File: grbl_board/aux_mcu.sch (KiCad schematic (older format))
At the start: 56 parts, among them J17 USB_B, J18 ICSP, Q5 BSS127S, Q6 BSS127S, Q7 BSS127S, SW2 SW_Push, U25 FT231XS, U26 40106, U27 74LS155, U28 ATmega328P-AU, U29 40106, U30 40106, U31 74LS153, U32 74LS153, Y2 16M

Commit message: complete footprint associations
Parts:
- removed U29, U30: 40106, symbol 4xxx:40106
- added unit 2 of U26
- added unit 3 of U26
- D47, D48: footprint (none) -> LED_SMD:LED_1206_3216Metric_Pad1.42x1.75mm_HandSolder; Digikey Part No. (none) -> 404-1042-1-ND
- U26: footprint (none) -> Package_SO:TSSOP-14_4.4x5mm_P0.65mm; Digikey Part No. (none) -> HEF40106BTT,112-ND
- U27: footprint (none) -> Package_SO:SOIC-16_3.9x9.9mm_P1.27mm; Digikey Part No. (none) -> 296-33960-5-ND
- U28: Digikey Part No. (none) -> ATMEGA328P-AU-ND
- U29: renamed from U31; footprint (none) -> Package_SO:SOIC-16_3.9x9.9mm_P1.27mm; Digikey Part No. (none) -> 296-3653-5-ND
- U30: renamed from U32; footprint (none) -> Package_SO:SOIC-16_3.9x9.9mm_P1.27mm; Digikey Part No. (none) -> 296-3653-5-ND
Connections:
- net Y_EN: now also U26.4
- net Z_EN: now also U26.6
- net at U27.10 (Q1b): now also U26.3
- net at U27.11 (Q2b): now also U26.5
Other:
- note added: "RXLED"
- note added: "TXLED"
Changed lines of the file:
@@
 F 2 "Package_QFP:TQFP-32_7x7mm_P0.8mm" H 5300 2650 50  0001 C CIN
 F 3 "http://ww1.microchip.com/downloads/en/DeviceDoc/ATmega328_P%20AVR%20MCU%20with%20picoPower%20Technology%20Data%20Sheet%2040001984A.pdf" H 5300 2650 50  0001 C CNN
+F 4 "ATMEGA328P-AU-ND" H 5300 2650 50  0001 C CNN "Digikey Part No."
 	1    5300 2650
 	1    0    0    -1
@@
 F 0 "D47" V 3547 6280 50  0000 L CNN
 F 1 "LED" V 3638 6280 50  0000 L CNN
-F 2 "" H 3600 6200 50  0001 C CNN
-F 3 "~" H 3600 6200 50  0001 C CNN
+F 2 "LED_SMD:LED_1206_3216Metric_Pad1.42x1.75mm_HandSolder" H 3600 6200 50  0001 C CNN
+F 3 "https://media.digikey.com/pdf/Data%20Sheets/Stanley%20Electric%20PDFs/1101W_Series.pdf" H 3600 6200 50  0001 C CNN
+F 4 "404-1042-1-ND" H 3600 6200 50  0001 C CNN "Digikey Part No."
 	1    3600 6200
 	0    1    1    0
@@
 F 0 "D48" V 3897 6280 50  0000 L CNN
 F 1 "LED" V 3988 6280 50  0000 L CNN
-F 2 "" H 3950 6200 50  0001 C CNN
-F 3 "~" H 3950 6200 50  0001 C CNN
+F 2 "LED_SMD:LED_1206_3216Metric_Pad1.42x1.75mm_HandSolder" H 3950 6200 50  0001 C CNN
+F 3 "https://media.digikey.com/pdf/Data%20Sheets/Stanley%20Electric%20PDFs/1101W_Series.pdf" H 3950 6200 50  0001 C CNN
+F 4 "404-1042-1-ND" H 3950 6200 50  0001 C CNN "Digikey Part No."
 	1    3950 6200
 	0    1    1    0
@@
 F 0 "U27" H 5350 7050 50  0000 C CNN
 F 1 "74LS155" H 5450 6950 50  0000 C CNN
-F 2 "" H 5200 6350 50  0001 C CNN
+F 2 "Package_SO:SOIC-16_3.9x9.9mm_P1.27mm" H 5200 6350 50  0001 C CNN
 F 3 "http://www.ti.com/lit/gpn/sn74LS155" H 5200 6350 50  0001 C CNN
+F 4 "296-33960-5-ND" H 5200 6350 50  0001 C CNN "Digikey Part No."
 	1    5200 6350
 	1    0    0    -1
@@
 F 0 "U26" H 6200 6367 50  0000 C CNN
 F 1 "40106" H 6200 6276 50  0000 C CNN
-F 2 "" H 6200 6050 50  0001 C CNN
+F 2 "Package_SO:TSSOP-14_4.4x5mm_P0.65mm" H 6200 6050 50  0001 C CNN
 F 3 "https://assets.nexperia.com/documents/data-sheet/HEF40106B.pdf" H 6200 6050 50  0001 C CNN
+F 4 "HEF40106BTT,112-ND" H 6200 6050 50  0001 C CNN "Digikey Part No."
 	1    6200 6050
-	1    0    0    -1
-$EndComp
-$Comp
-L 4xxx:40106 U29
-U 1 1 6201B7B4
-P 6200 6550
-F 0 "U29" H 6200 6867 50  0000 C CNN
-F 1 "40106" H 6200 6776 50  0000 C CNN
-F 2 "" H 6200 6550 50  0001 C CNN
-F 3 "https://assets.nexperia.com/documents/data-sheet/HEF40106B.pdf" H 6200 6550 50  0001 C CNN
-	1    6200 6550
-	1    0    0    -1
-$EndComp
-$Comp
-L 4xxx:40106 U30
-U 1 1 62027074
-P 6200 7050
-F 0 "U30" H 6200 7367 50  0000 C CNN
-F 1 "40106" H 6200 7276 50  0000 C CNN
-F 2 "" H 6200 7050 50  0001 C CNN
-F 3 "https://assets.nexperia.com/documents/data-sheet/HEF40106B.pdf" H 6200 7050 50  0001 C CNN
-	1    6200 7050
 	1    0    0    -1
 $EndComp
@@
 F 0 "U26" H 4430 3296 50  0000 L CNN
 F 1 "40106" H 4430 3205 50  0000 L CNN
-F 2 "" H 4200 3250 50  0001 C CNN
+F 2 "Package_SO:TSSOP-14_4.4x5mm_P0.65mm" H 4200 3250 50  0001 C CNN
 F 3 "https://assets.nexperia.com/documents/data-sheet/HEF40106B.pdf" H 4200 3250 50  0001 C CNN
+F 4 "HEF40106BTT,112-ND" H 4200 3250 50  0001 C CNN "Digikey Part No."
 	7    4200 3250
 	1    0    0    -1
@@
 $EndComp
 $Comp
-L 74xx:74LS153 U31
+L 74xx:74LS153 U29
 U 1 1 618CA113
 P 8350 4300
-F 0 "U31" H 8500 5300 50  0000 C CNN
+F 0 "U29" H 8500 5300 50  0000 C CNN
 F 1 "74LS153" H 8600 5200 50  0000 C CNN
-F 2 "" H 8350 4300 50  0001 C CNN
+F 2 "Package_SO:SOIC-16_3.9x9.9mm_P1.27mm" H 8350 4300 50  0001 C CNN
 F 3 "http://www.ti.com/lit/gpn/sn74LS153" H 8350 4300 50  0001 C CNN
+F 4 "296-3653-5-ND" H 8350 4300 50  0001 C CNN "Digikey Part No."
 	1    8350 4300
 	1    0    0    -1
@@
 	7850 5100 6950 5100
 $Comp
-L 74xx:74LS153 U32
+L 74xx:74LS153 U30
 U 1 1 61E49967
 P 10450 4700
-F 0 "U32" H 10600 5700 50  0000 C CNN
+F 0 "U30" H 10600 5700 50  0000 C CNN
 F 1 "74LS153" H 10700 5600 50  0000 C CNN
-F 2 "" H 10450 4700 50  0001 C CNN
+F 2 "Package_SO:SOIC-16_3.9x9.9mm_P1.27mm" H 10450 4700 50  0001 C CNN
 F 3 "http://www.ti.com/lit/gpn/sn74LS153" H 10450 4700 50  0001 C CNN
+F 4 "296-3653-5-ND" H 10450 4700 50  0001 C CNN "Digikey Part No."
 	1    10450 4700
 	1    0    0    -1
@@
 	1    0    0    -1
 $EndComp
+$Comp
+L 4xxx:40106 U26
+U 2 1 61AE43E8
+P 6200 6550
+F 0 "U26" H 6200 6867 50  0000 C CNN
+F 1 "40106" H 6200 6776 50  0000 C CNN
+F 2 "Package_SO:TSSOP-14_4.4x5mm_P0.65mm" H 6200 6550 50  0001 C CNN
+F 3 "https://assets.nexperia.com/documents/data-sheet/HEF40106B.pdf" H 6200 6550 50  0001 C CNN
+F 4 "HEF40106BTT,112-ND" H 6200 6550 50  0001 C CNN "Digikey Part No."
+	2    6200 6550
+	1    0    0    -1
+$EndComp
+$Comp
+L 4xxx:40106 U26
+U 3 1 61AE6394
+P 6200 7050
+F 0 "U26" H 6200 7367 50  0000 C CNN
+F 1 "40106" H 6200 7276 50  0000 C CNN
+F 2 "Package_SO:TSSOP-14_4.4x5mm_P0.65mm" H 6200 7050 50  0001 C CNN
+F 3 "https://assets.nexperia.com/documents/data-sheet/HEF40106B.pdf" H 6200 7050 50  0001 C CNN
+F 4 "HEF40106BTT,112-ND" H 6200 7050 50  0001 C CNN "Digikey Part No."
+	3    6200 7050
+	1    0    0    -1
+$EndComp
+Text Notes 4000 6000 0    50   ~ 0
+TXLED
+Text Notes 3650 6000 0    50   ~ 0
+RXLED
 $EndSCHEMATC

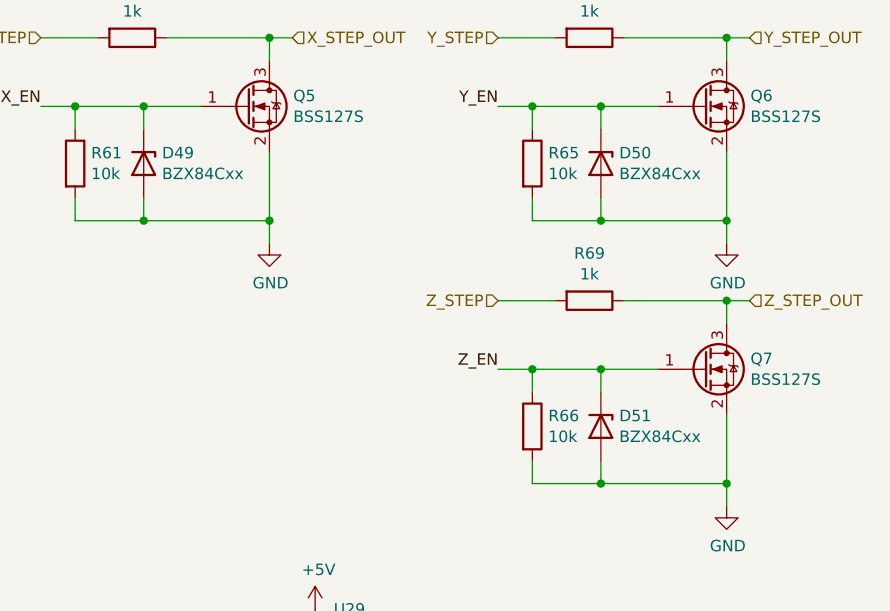
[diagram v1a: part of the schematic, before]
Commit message: fixed mismatch for 6n137
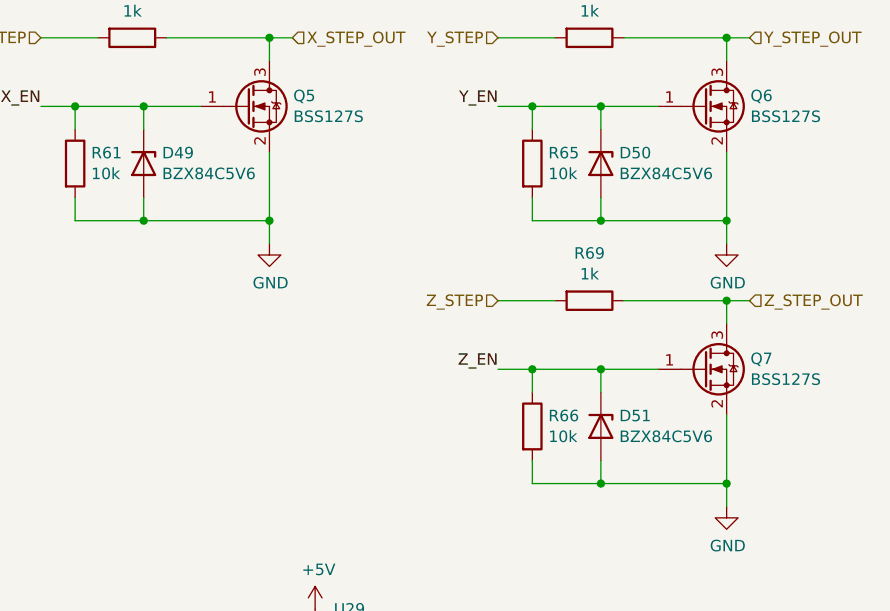
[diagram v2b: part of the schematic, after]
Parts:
- D49, D50, D51: value BZX84Cxx -> BZX84C5V6; Digikey Part No. (none) -> 1514-BZX84C5V6TRPBFREECT-ND
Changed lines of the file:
@@
 P 7600 1350
 F 0 "D49" V 7554 1430 50  0000 L CNN
-F 1 "BZX84Cxx" V 7645 1430 50  0000 L CNN
+F 1 "BZX84C5V6" V 7645 1430 50  0000 L CNN
 F 2 "Diode_SMD:D_SOT-23_ANK" H 7600 1175 50  0001 C CNN
 F 3 "https://diotec.com/tl_files/diotec/files/pdf/datasheets/bzx84c2v4.pdf" H 7600 1350 50  0001 C CNN
+F 4 "1514-BZX84C5V6TRPBFREECT-ND" H 7600 1350 50  0001 C CNN "Digikey Part No."
 	1    7600 1350
 	0    1    1    0
@@
 P 9600 1350
 F 0 "D50" V 9554 1430 50  0000 L CNN
-F 1 "BZX84Cxx" V 9645 1430 50  0000 L CNN
+F 1 "BZX84C5V6" V 9645 1430 50  0000 L CNN
 F 2 "Diode_SMD:D_SOT-23_ANK" H 9600 1175 50  0001 C CNN
 F 3 "https://diotec.com/tl_files/diotec/files/pdf/datasheets/bzx84c2v4.pdf" H 9600 1350 50  0001 C CNN
+F 4 "1514-BZX84C5V6TRPBFREECT-ND" H 9600 1350 50  0001 C CNN "Digikey Part No."
 	1    9600 1350
 	0    1    1    0
@@
 P 9600 2500
 F 0 "D51" V 9554 2580 50  0000 L CNN
-F 1 "BZX84Cxx" V 9645 2580 50  0000 L CNN
+F 1 "BZX84C5V6" V 9645 2580 50  0000 L CNN
 F 2 "Diode_SMD:D_SOT-23_ANK" H 9600 2325 50  0001 C CNN
 F 3 "https://diotec.com/tl_files/diotec/files/pdf/datasheets/bzx84c2v4.pdf" H 9600 2500 50  0001 C CNN
+F 4 "1514-BZX84C5V6TRPBFREECT-ND" H 9600 2500 50  0001 C CNN "Digikey Part No."
 	1    9600 2500
 	0    1    1    0
